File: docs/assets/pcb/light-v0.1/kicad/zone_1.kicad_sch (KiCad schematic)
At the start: 13 parts, among them J2 ZONE 1, Q101 AO3422, Q102 AO3422, Q103 AO3422

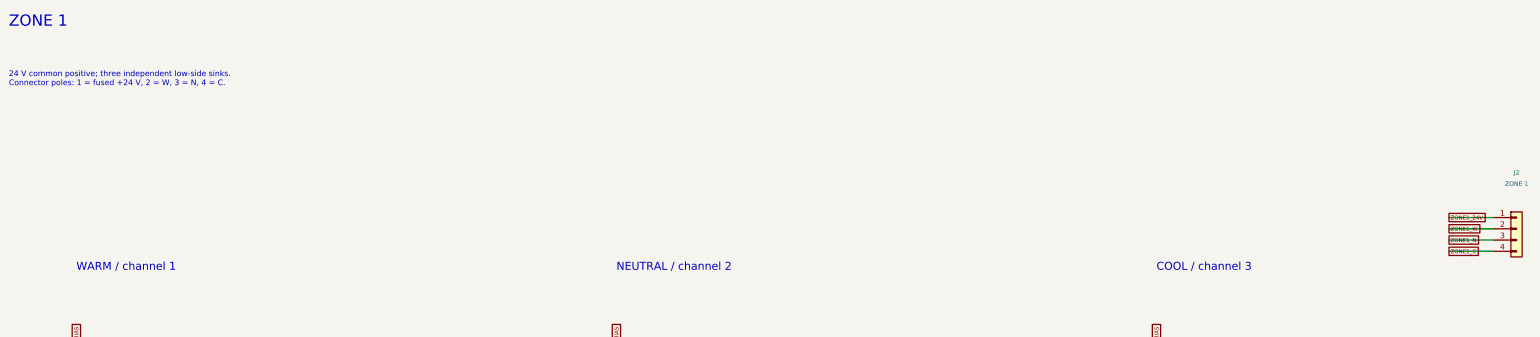
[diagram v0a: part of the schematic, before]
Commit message: Refresh PCB chapters from verified central LED snapshots
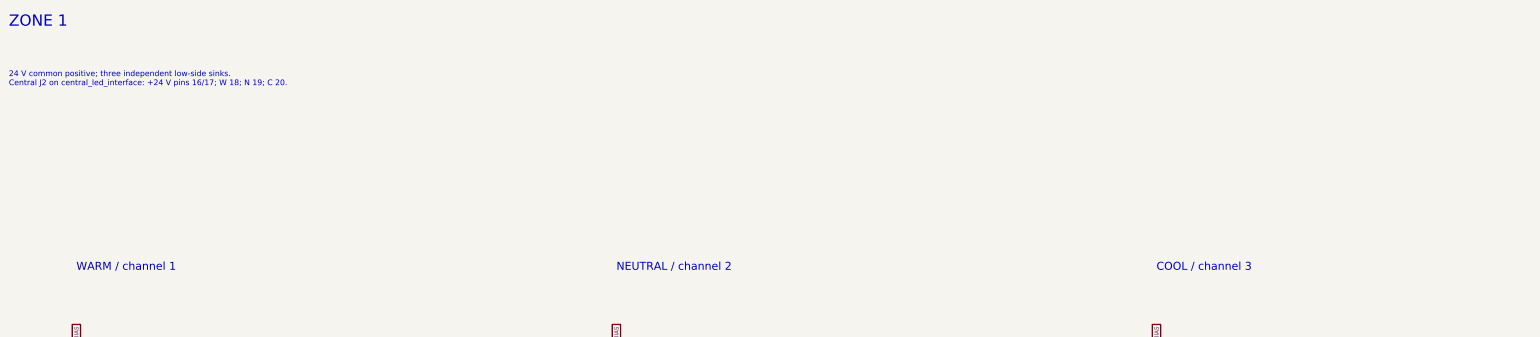
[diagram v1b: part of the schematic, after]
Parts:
- removed J2: ZONE 1, Connector_JST:JST_GH_SM04B-GHS-TB_1x04-1MP_P1.25mm_Horizontal, symbol Connector_Generic:Conn_01x04
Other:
- note added: "24 V common positive; three independent low-side sinks. Central J2 on central_led_interface: +24 V pins 16/17; W 18; N 19; C 20."
- note removed: "24 V common positive; three independent low-side sinks. Connector poles: 1 = fused +24 V, 2 = W, 3 = N, 4 = C."
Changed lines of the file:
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@@
   (title_block
     (title "Zone 1")
-    (date "2026-09-06")
-    (rev "A draft")
+    (date "2026-09-08")
+    (rev "LIGHT v0.2 candidate")
     (company "Engineered Lighting")
     (comment 1 "ENGINEERING DRAFT - see release status before fabrication"))
-  (symbol
-    (lib_id "Connector_Generic:Conn_01x04")
-    (at 360.68 63.5 0)
-    (unit 1)
-    (exclude_from_sim yes)
-    (in_bom yes)
-    (on_board yes)
-    (dnp no)
-    (property "Reference" "J2"
-      (at 360.68 50.8 0.0)
-      (effects
-        (font
-          (size 1.0 1.0))))
-    (property "Value" "ZONE 1"
-      (at 360.68 53.34 0.0)
-      (effects
-        (font
-          (size 1.0 1.0))))
-    (property "Footprint" "Connector_JST:JST_GH_SM04B-GHS-TB_1x04-1MP_P1.25mm_Horizontal"
-      (at 360.68 63.5 0.0)
-      (hide yes)
-      (effects
-        (font
-          (size 1.0 1.0))))
-    (property "MPN" "SM04B-GHS-TB(LF)(SN)"
-      (at 360.68 63.5 0.0)
-      (hide yes)
-      (effects
-        (font
-          (size 1.0 1.0))))
-    (property "Manufacturer" "JST"
-      (at 360.68 63.5 0.0)
-      (hide yes)
-      (effects
-        (font
-          (size 1.0 1.0))))
-    (property "Datasheet" ""
-      (at 360.68 63.5 0.0)
-      (hide yes)
-      (effects
-        (font
-          (size 1.0 1.0))))
-    (instances
-      (project "engineered-lighting-rev-a"
-        (path "/964013ac-cca6-5de7-b648-d598a25a58e0/5ff23d2b-ccbd-5c4e-8f47-def758dc135b"
-          (reference "J2")
-          (unit 1))))
-    (pin "1"
-)
-    (pin "2"
-)
-    (pin "3"
-)
-    (pin "4"
-))
-  (wire
-    (pts
-      (xy 355.6 60.96)
-      (xy 345.44 60.96))
-    (stroke
-      (width 0)
-      (type default))
-)
-  (global_label "ZONE1_24V"
-    (shape passive)
-    (at 345.44 60.96 0.0)
-    (effects
-      (font
-        (size 0.9 0.9))
-      (justify left))
-    (property "Intersheetrefs" "${INTERSHEET_REFS}"
-      (at 345.44 60.96 0.0)
-      (hide yes)
-      (effects
-        (font
-          (size 1.0 1.0)))))
-  (wire
-    (pts
-      (xy 355.6 63.5)
-      (xy 345.44 63.5))
-    (stroke
-      (width 0)
-      (type default))
-)
-  (global_label "ZONE1_W"
-    (shape passive)
-    (at 345.44 63.5 0.0)
-    (effects
-      (font
-        (size 0.9 0.9))
-      (justify left))
-    (property "Intersheetrefs" "${INTERSHEET_REFS}"
-      (at 345.44 63.5 0.0)
-      (hide yes)
-      (effects
-        (font
-          (size 1.0 1.0)))))
-  (wire
-    (pts
-      (xy 355.6 66.04)
-      (xy 345.44 66.04))
-    (stroke
-      (width 0)
-      (type default))
-)
-  (global_label "ZONE1_N"
-    (shape passive)
-    (at 345.44 66.04 0.0)
-    (effects
-      (font
-        (size 0.9 0.9))
-      (justify left))
-    (property "Intersheetrefs" "${INTERSHEET_REFS}"
-      (at 345.44 66.04 0.0)
-      (hide yes)
-      (effects
-        (font
-          (size 1.0 1.0)))))
-  (wire
-    (pts
-      (xy 355.6 68.58)
-      (xy 345.44 68.58))
-    (stroke
-      (width 0)
-      (type default))
-)
-  (global_label "ZONE1_C"
-    (shape passive)
-    (at 345.44 68.58 0.0)
-    (effects
-      (font
-        (size 0.9 0.9))
-      (justify left))
-    (property "Intersheetrefs" "${INTERSHEET_REFS}"
-      (at 345.44 68.58 0.0)
-      (hide yes)
-      (effects
-        (font
-          (size 1.0 1.0)))))
   (symbol
     (lib_id "EL:AO3422")
@@
       (justify left top))
 )
-  (text "24 V common positive; three independent low-side sinks.\nConnector poles: 1 = fused +24 V, 2 = W, 3 = N, 4 = C."
+  (text "24 V common positive; three independent low-side sinks.\nCentral J2 on central_led_interface: +24 V pins 16/17; W 18; N 19; C 20."
     (at 20.32 27.94 0)
     (effects
